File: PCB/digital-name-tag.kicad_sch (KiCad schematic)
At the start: 33 parts, among them J1 USB_C_Receptacle_USB2.0_14P, J2 Conn_01x20, J3 Conn_01x20, J4 Conn_01x03, SW1 SW_Push, U1 RP2040, U2 MCP1700x-120xxMB, U3 W25Q128JVS, Y1 12MHz

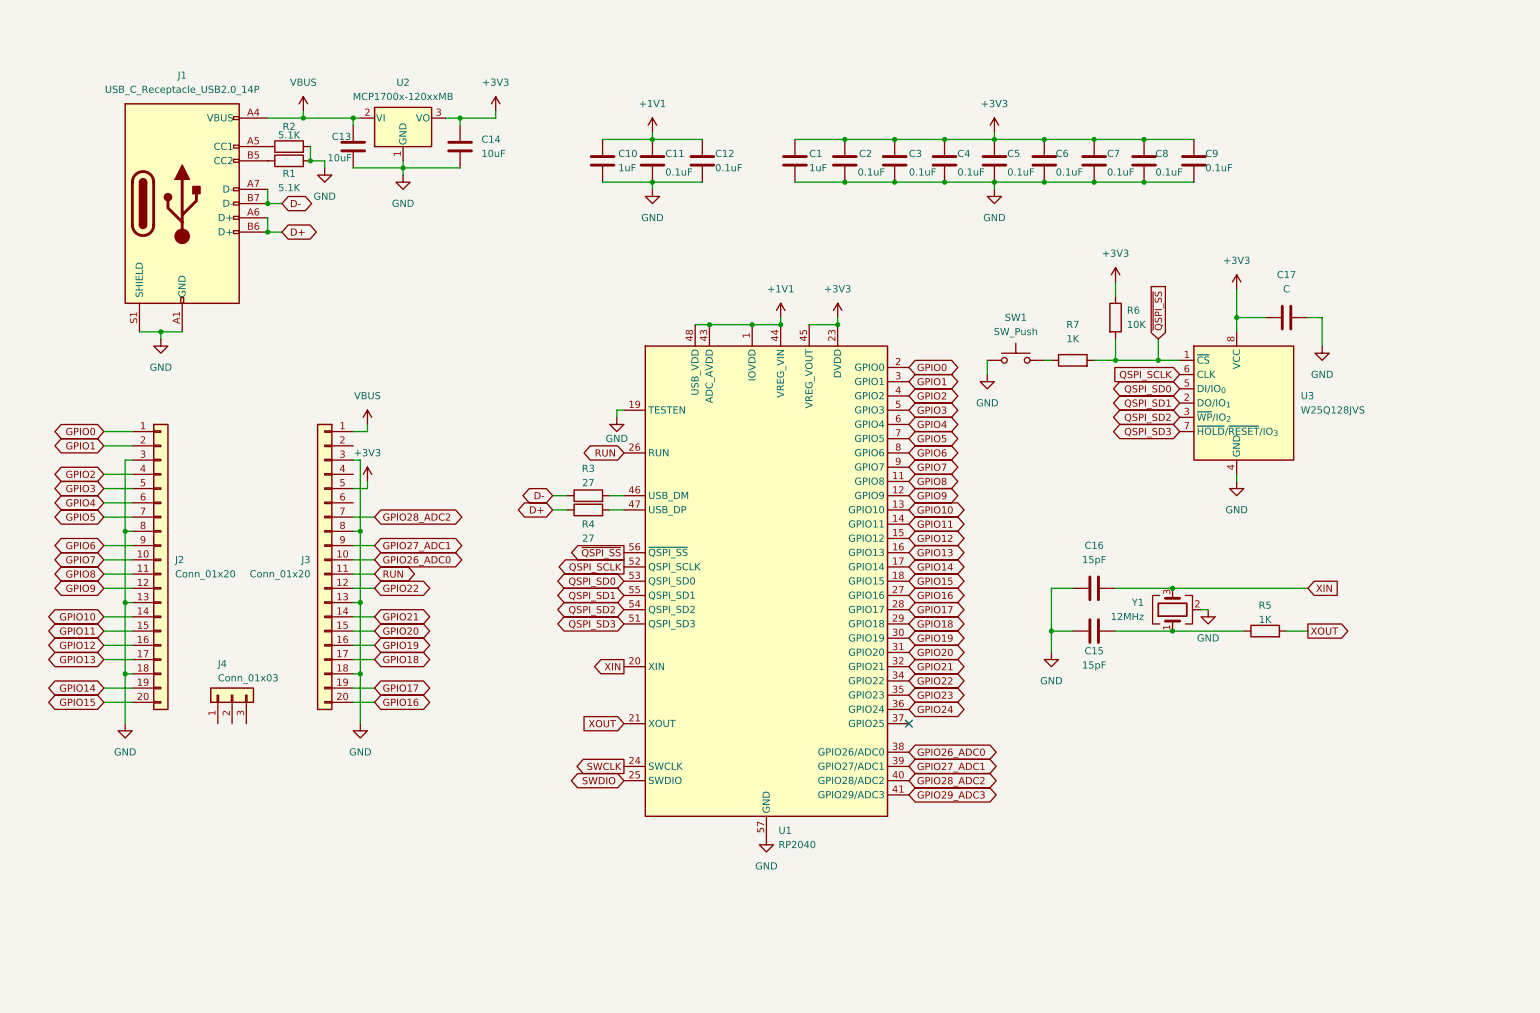
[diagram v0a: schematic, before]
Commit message: finished seting up the schematic and assigned all the footprints
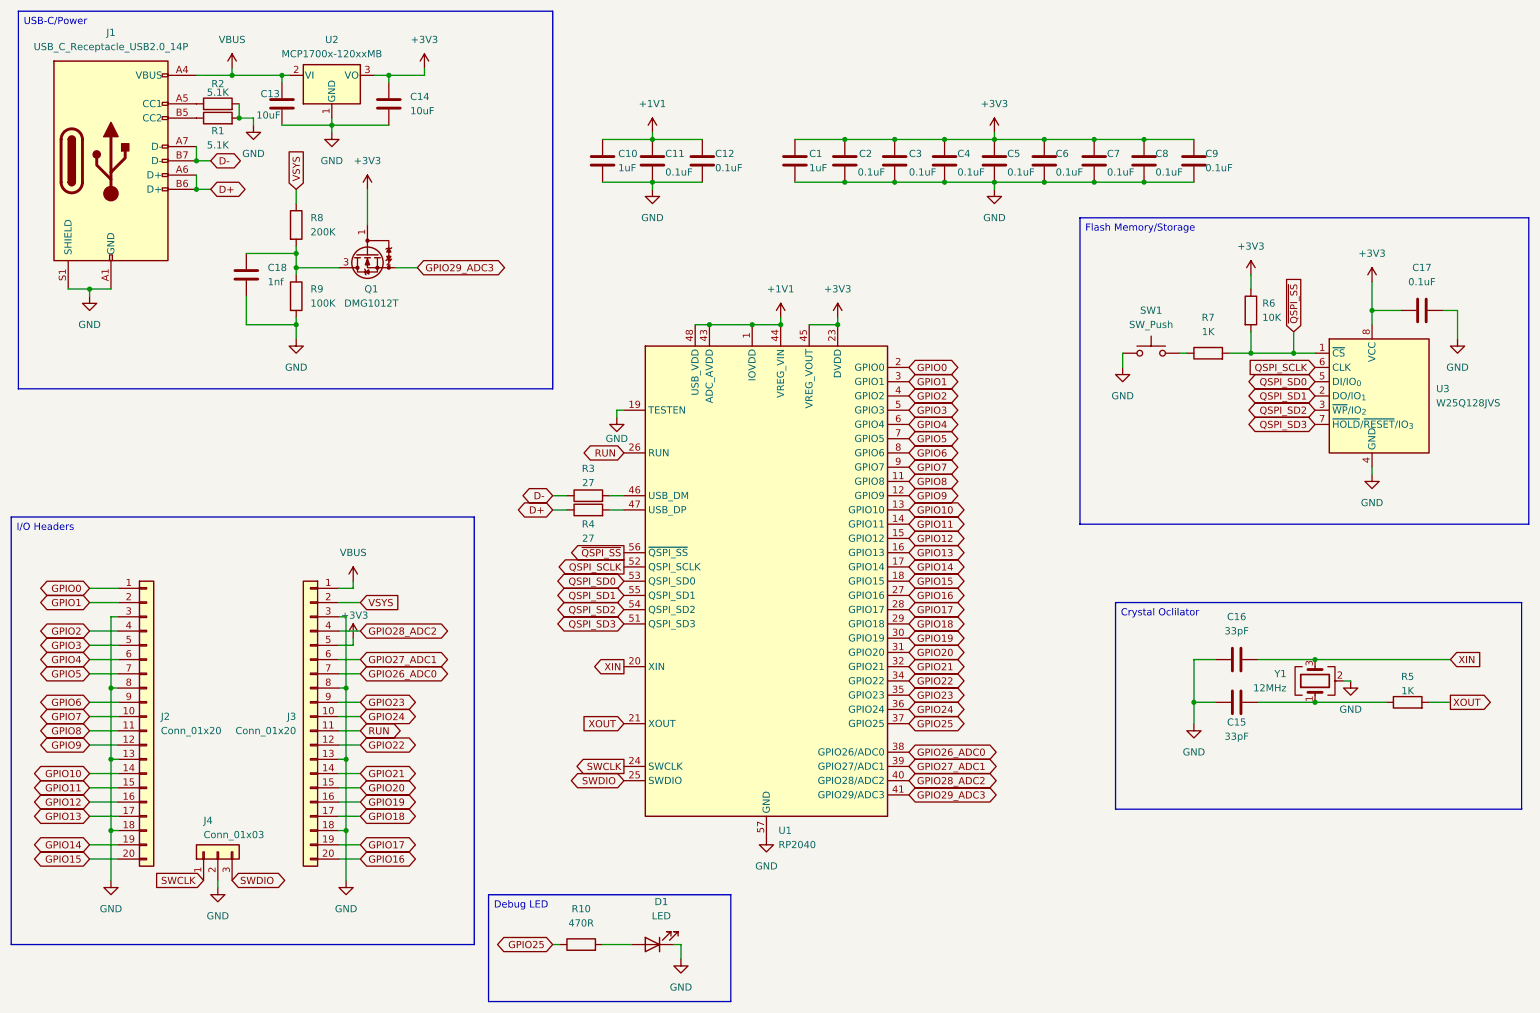
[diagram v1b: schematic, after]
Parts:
- added C18: 1nf, Capacitor_SMD:C_0402_1005Metric, symbol Device:C
- added D1: LED, LED_SMD:LED_0603_1608Metric, symbol Device:LED
- added Q1: DMG1012T, Package_TO_SOT_SMD:SOT-523, symbol Transistor_FET:DMG1012T
- added R10: 470R, Capacitor_SMD:C_01005_0402Metric, symbol Device:R
- added R8: 200K, Capacitor_SMD:C_01005_0402Metric, symbol Device:R
- added R9: 100K, Capacitor_SMD:C_01005_0402Metric, symbol Device:R
- C1, C10, C11, C12, C2, C3, C4, C5, C6, C7, C8, C9: footprint (none) -> Capacitor_SMD:C_0402_1005Metric
- C13, C14: footprint (none) -> Capacitor_SMD:C_0603_1608Metric
- C15, C16: value 15pF -> 33pF; footprint (none) -> Capacitor_SMD:C_0603_1608Metric; lcsc part # (none) -> C1663
- C17: value C -> 0.1uF; footprint (none) -> Capacitor_SMD:C_0402_1005Metric
- J1: footprint (none) -> Connector_USB:USB_C_Receptacle_HRO_TYPE-C-31-M-12
- J2, J3: footprint (none) -> Connector_PinHeader_2.54mm:PinHeader_1x20_P2.54mm_Vertical
- J4: footprint (none) -> Connector_PinHeader_2.54mm:PinHeader_1x03_P2.54mm_Vertical
- R1, R2, R3, R4, R5, R6, R7: footprint (none) -> Capacitor_SMD:C_01005_0402Metric
- SW1: footprint (none) -> Button_Switch_SMD:SW_Push_SPST_NO_Alps_SKRK
- Y1: footprint (none) -> Crystal:Crystal_SMD_3225-4Pin_3.2x2.5mm; lcsc part # (none) -> C9002
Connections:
- net +3V3: now also Q1.1 (G)
- net GND: now also J4.2 (Pin_2), C18.2, D1.1 (K), R9.2
- net GPIO23: now also J3.9 (Pin_9)
- net GPIO24: now also J3.10 (Pin_10)
- net GPIO26_ADC0: now also J3.7 (Pin_7); no longer J3.10 (Pin_10)
- net GPIO27_ADC1: now also J3.6 (Pin_6); no longer J3.9 (Pin_9)
- net GPIO28_ADC2: now also J3.4 (Pin_4); no longer J3.7 (Pin_7)
- net GPIO29_ADC3: now also Q1.2 (S)
- net SWCLK: now also J4.1 (Pin_1)
- net SWDIO: now also J4.3 (Pin_3)
- net GPIO25: now reaches U1.37 (GPIO25)
- net GPIO25: now also R10.1
- net VSYS: now reaches J3.2 (Pin_2)
- net VSYS: now also R8.1
- new net: D1.2 (A), R10.2
- new net: C18.1, Q1.3 (D), R8.2, R9.1
- no-connect marks 1 -> 0
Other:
- moved on the sheet: C13, C14, C15, C16, C17, J1, J2, J3, J4, R1, R2, R5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

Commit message: startet placing footpints and updated limage links for JOURNAL.md
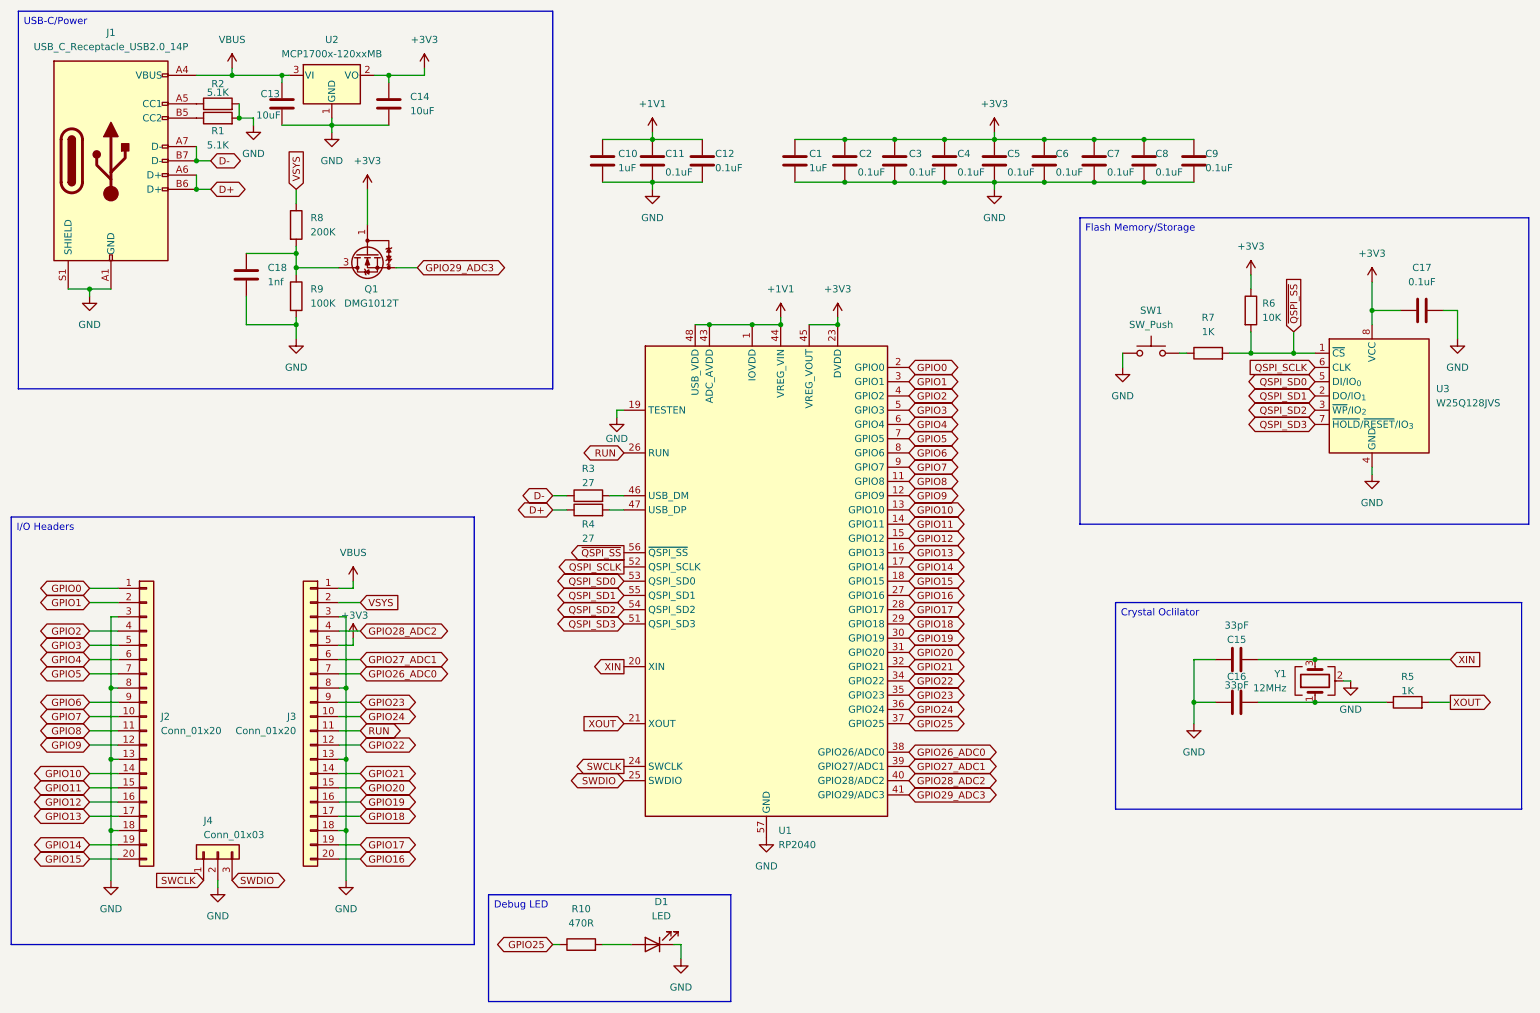
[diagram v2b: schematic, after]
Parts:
- C15, C16: footprint Capacitor_SMD:C_0603_1608Metric -> Capacitor_SMD:C_0402_1005Metric
- U2: footprint Package_TO_SOT_SMD:SOT-89-3 -> Package_TO_SOT_SMD:SOT-23; symbol Regulator_Linear:MCP1700x-120xxMB -> Regulator_Linear:MCP1700x-330xxTT
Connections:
- net +3V3: now also U2.2 (VO); no longer U2.3 (VO)
- net GND: now also C15.1; no longer C15.2
- net VBUS: now also U2.3 (VI); no longer U2.2 (VI)
- net XIN: now also C15.2; no longer C16.2
- net at R5.1, Y1.1: now also C16.2; no longer C15.1
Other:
- moved on the sheet: C15, C16
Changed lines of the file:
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@@
 	)
 	(junction
+		(at 245.11 129.54)
+		(diameter 0)
+		(color 0 0 0 0)
+	)
+	(junction
 		(at 63.5 59.69)
 		(diameter 0)
@@
 	)
 	(junction
-		(at 245.11 129.54)
-		(diameter 0)
-		(color 0 0 0 0)
-	)
-	(junction
 		(at 214.63 44.45)
 		(diameter 0)
@@
 	)
 	(junction
-		(at 60.96 25.4)
+		(at 223.52 137.16)
 		(diameter 0)
 		(color 0 0 0 0)
 	)
 	(junction
-		(at 241.3 74.93)
+		(at 60.96 25.4)
 		(diameter 0)
 		(color 0 0 0 0)
 	)
 	(junction
-		(at 80.01 25.4)
+		(at 241.3 74.93)
 		(diameter 0)
 		(color 0 0 0 0)
 	)
 	(junction
-		(at 223.52 137.16)
+		(at 80.01 25.4)
 		(diameter 0)
 		(color 0 0 0 0)
@@
 	(wire
 		(pts
+			(xy 223.52 129.54) (xy 227.33 129.54)
+		)
+		(stroke
+			(width 0)
+			(type default)
+		)
+	)
+	(wire
+		(pts
 			(xy 26.67 152.4) (xy 31.75 152.4)
 		)
@@
 	(wire
 		(pts
-			(xy 223.52 129.54) (xy 223.52 137.16)
+			(xy 54.61 69.85) (xy 63.5 69.85)
 		)
 		(stroke
@@
 	(wire
 		(pts
-			(xy 54.61 69.85) (xy 63.5 69.85)
+			(xy 132.08 180.34) (xy 132.08 182.88)
 		)
 		(stroke
@@
 	(wire
 		(pts
-			(xy 132.08 180.34) (xy 132.08 182.88)
+			(xy 245.11 129.54) (xy 269.24 129.54)
 		)
 		(stroke
@@
 	(wire
 		(pts
-			(xy 245.11 129.54) (xy 269.24 129.54)
+			(xy 60.96 25.4) (xy 62.23 25.4)
 		)
 		(stroke
@@
 	(wire
 		(pts
-			(xy 223.52 137.16) (xy 227.33 137.16)
+			(xy 73.66 127) (xy 71.12 127)
 		)
 		(stroke
@@
 	(wire
 		(pts
-			(xy 60.96 25.4) (xy 62.23 25.4)
+			(xy 26.67 139.7) (xy 31.75 139.7)
 		)
 		(stroke
@@
 	(wire
 		(pts
-			(xy 73.66 127) (xy 71.12 127)
+			(xy 223.52 129.54) (xy 223.52 137.16)
 		)
 		(stroke
@@
 	(wire
 		(pts
-			(xy 26.67 139.7) (xy 31.75 139.7)
+			(xy 160.02 68.58) (xy 160.02 69.85)
 		)
 		(stroke
@@
 	(wire
 		(pts
-			(xy 160.02 68.58) (xy 160.02 69.85)
+			(xy 45.72 38.1) (xy 45.72 40.64)
 		)
 		(stroke
@@
 	(wire
 		(pts
-			(xy 45.72 38.1) (xy 45.72 40.64)
+			(xy 214.63 44.45) (xy 223.52 44.45)
 		)
 		(stroke
@@
 	(wire
 		(pts
-			(xy 214.63 44.45) (xy 223.52 44.45)
+			(xy 69.85 35.56) (xy 69.85 34.29)
 		)
 		(stroke
@@
 	(wire
 		(pts
-			(xy 69.85 35.56) (xy 69.85 34.29)
+			(xy 234.95 137.16) (xy 245.11 137.16)
 		)
 		(stroke
@@
 	(wire
 		(pts
+			(xy 234.95 129.54) (xy 245.11 129.54)
+		)
+		(stroke
+			(width 0)
+			(type default)
+		)
+	)
+	(wire
+		(pts
 			(xy 109.22 100.33) (xy 111.76 100.33)
 		)
@@
 	(wire
 		(pts
+			(xy 223.52 137.16) (xy 223.52 140.97)
+		)
+		(stroke
+			(width 0)
+			(type default)
+		)
+	)
+	(wire
+		(pts
 			(xy 187.96 36.83) (xy 196.85 36.83)
 		)
@@
 	(wire
 		(pts
-			(xy 71.12 160.02) (xy 72.39 160.02)
-		)
-		(stroke
-			(width 0)
-			(type default)
-		)
-	)
-	(wire
-		(pts
-			(xy 86.36 25.4) (xy 80.01 25.4)
+			(xy 223.52 137.16) (xy 227.33 137.16)
 		)
 		(stroke
@@
 	(wire
 		(pts
-			(xy 118.11 180.34) (xy 123.19 180.34)
+			(xy 71.12 160.02) (xy 72.39 160.02)
 		)
 		(stroke
@@
 	(wire
 		(pts
-			(xy 60.96 34.29) (xy 69.85 34.29)
+			(xy 86.36 25.4) (xy 80.01 25.4)
 		)
 		(stroke
@@
 	(wire
 		(pts
-			(xy 73.66 125.73) (xy 73.66 127)
+			(xy 118.11 180.34) (xy 123.19 180.34)
 		)
 		(stroke
@@
 	(wire
 		(pts
-			(xy 187.96 35.56) (xy 187.96 36.83)
+			(xy 60.96 34.29) (xy 69.85 34.29)
 		)
 		(stroke
@@
 	(wire
 		(pts
-			(xy 26.67 162.56) (xy 31.75 162.56)
+			(xy 73.66 125.73) (xy 73.66 127)
 		)
 		(stroke
@@
 	(wire
 		(pts
-			(xy 223.52 137.16) (xy 223.52 140.97)
+			(xy 187.96 35.56) (xy 187.96 36.83)
 		)
 		(stroke
@@
 	(wire
 		(pts
-			(xy 227.33 129.54) (xy 223.52 129.54)
+			(xy 26.67 162.56) (xy 31.75 162.56)
 		)
 		(stroke
@@
 	(wire
 		(pts
-			(xy 234.95 129.54) (xy 245.11 129.54)
-		)
-		(stroke
-			(width 0)
-			(type default)
-		)
-	)
-	(wire
-		(pts
 			(xy 63.5 55.88) (xy 63.5 57.15)
 		)
@@
 	(wire
 		(pts
-			(xy 234.95 137.16) (xy 245.11 137.16)
-		)
-		(stroke
-			(width 0)
-			(type default)
-		)
-	)
-	(wire
-		(pts
 			(xy 52.07 25.4) (xy 60.96 25.4)
 		)
@@
 	(symbol
 		(lib_id "Device:C")
-		(at 231.14 137.16 270)
+		(at 231.14 129.54 90)
 		(unit 1)
 		(exclude_from_sim no)
@@
 		(dnp no)
 		(property "Reference" "C15"
-			(at 231.14 140.716 90)
+			(at 231.14 125.984 90)
 			(effects
 				(font
@@
 		)
 		(property "Value" "33pF"
-			(at 231.14 143.256 90)
+			(at 231.14 123.444 90)
 			(effects
 				(font
@@
 			)
 		)
-		(property "Footprint" "Capacitor_SMD:C_0603_1608Metric"
-			(at 227.33 138.1252 0)
+		(property "Footprint" "Capacitor_SMD:C_0402_1005Metric"
+			(at 234.95 128.5748 0)
 			(effects
 				(font
@@
 		)
 		(property "Datasheet" "~"
-			(at 231.14 137.16 0)
+			(at 231.14 129.54 0)
 			(effects
 				(font
@@
 		)
 		(property "Description" "Unpolarized capacitor"
-			(at 231.14 137.16 0)
+			(at 231.14 129.54 0)
 			(effects
 				(font
@@
 		)
 		(property "lcsc part #" "C1663"
-			(at 231.14 137.16 90)
+			(at 231.14 129.54 90)
 			(effects
 				(font
@@
 	(symbol
 		(lib_id "Device:C")
-		(at 231.14 129.54 90)
+		(at 231.14 137.16 90)
 		(unit 1)
 		(exclude_from_sim no)
@@
 		(on_board yes)
 		(dnp no)
-		(fields_autoplaced yes)
 		(property "Reference" "C16"
-			(at 231.14 121.92 90)
+			(at 231.14 132.588 90)
 			(effects
 				(font
@@
 		)
 		(property "Value" "33pF"
-			(at 231.14 124.46 90)
+			(at 231.14 134.112 90)
 			(effects
 				(font
@@
 			)
 		)
-		(property "Footprint" "Capacitor_SMD:C_0603_1608Metric"
-			(at 234.95 128.5748 0)
+		(property "Footprint" "Capacitor_SMD:C_0402_1005Metric"
+			(at 234.95 136.1948 0)
 			(effects
 				(font
@@
 		)
 		(property "Datasheet" "~"
-			(at 231.14 129.54 0)
+			(at 231.14 137.16 0)
 			(effects
 				(font
@@
 		)
 		(property "Description" "Unpolarized capacitor"
-			(at 231.14 129.54 0)
+			(at 231.14 137.16 0)
 			(effects
 				(font
@@
 		)
 		(property "lcsc part #" "C1663"
-			(at 231.14 129.54 90)
+			(at 231.14 137.16 90)
 			(effects
 				(font
@@
 	)
 	(symbol
-		(lib_id "Regulator_Linear:MCP1700x-120xxMB")
+		(lib_id "Regulator_Linear:MCP1700x-330xxTT")
 		(at 69.85 25.4 0)
 		(unit 1)
@@
 			)
 		)
-		(property "Footprint" "Package_TO_SOT_SMD:SOT-89-3"
-			(at 69.85 20.32 0)
+		(property "Footprint" "Package_TO_SOT_SMD:SOT-23"
+			(at 69.85 19.685 0)
 			(effects
 				(font
@@
 		)
 		(property "Datasheet" "http://ww1.microchip.com/downloads/en/DeviceDoc/20001826D.pdf"
-			(at 69.85 26.67 0)
+			(at 69.85 25.4 0)
 			(effects
 				(font
@@
 			)
 		)
-		(property "Description" "250mA Low Quiscent Current LDO, 1.2V output, SOT-89"
+		(property "Description" "250mA Low Quiscent Current LDO, 3.3V output, SOT-23"
 			(at 69.85 25.4 0)
 			(effects

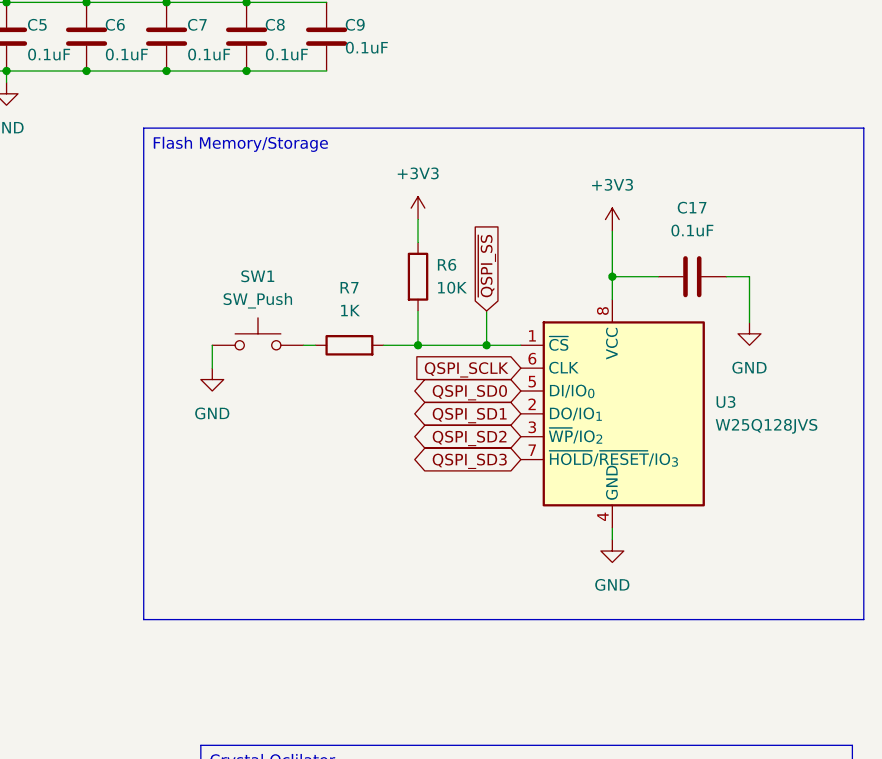
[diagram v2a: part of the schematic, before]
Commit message: finnished layout and mostly got routing done
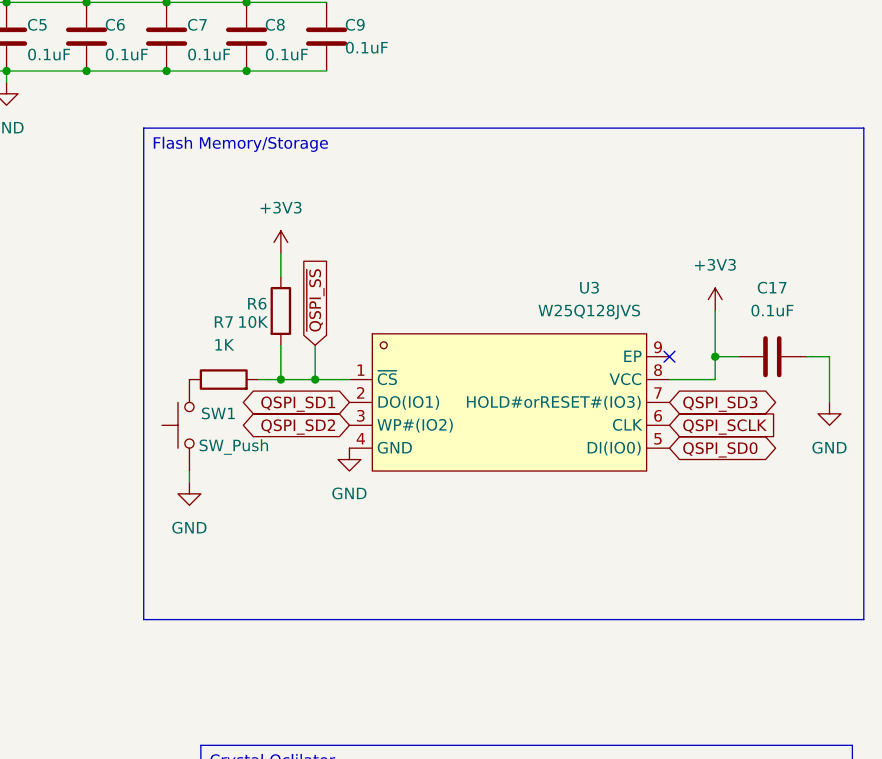
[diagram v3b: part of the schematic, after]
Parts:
- R1, R10, R2, R3, R4, R5, R6, R7, R8, R9: footprint Capacitor_SMD:C_01005_0402Metric -> Resistor_SMD:R_0402_1005Metric
- U3: footprint Package_SO:SOIC-8_5.3x5.3mm_P1.27mm -> easyeda2kicad:USON-8_L3.0-W2.0-P0.50-BL-EP; symbol Memory_Flash:W25Q128JVS -> easyeda2kicad:W25Q16JVUXIQ; LCSC Part (none) -> C2843335; MPN (none) -> W25Q16JVUXIQ; Manufacturer (none) -> Winbond(华邦)
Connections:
- no-connect marks 0 -> 1
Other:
- moved on the sheet: C17, R6, R7, SW1

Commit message: fixed DRC errors
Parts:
- R8: lcsc part # (none) -> C22369193
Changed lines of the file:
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@@
+			)
+		)
+		(property "lcsc part #" "C22369193"
+			(at 63.5 52.07 0)
+			(effects
+				(font
+					(size 1.27 1.27)
+				)
+				(hide yes)
 			)
 		)
